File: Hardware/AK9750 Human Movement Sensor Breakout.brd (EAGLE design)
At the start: 25.4 x 25.4 mm, 27 parts, among them J2 SMD, J3 PTH, J4 SMD, U2 AK9750

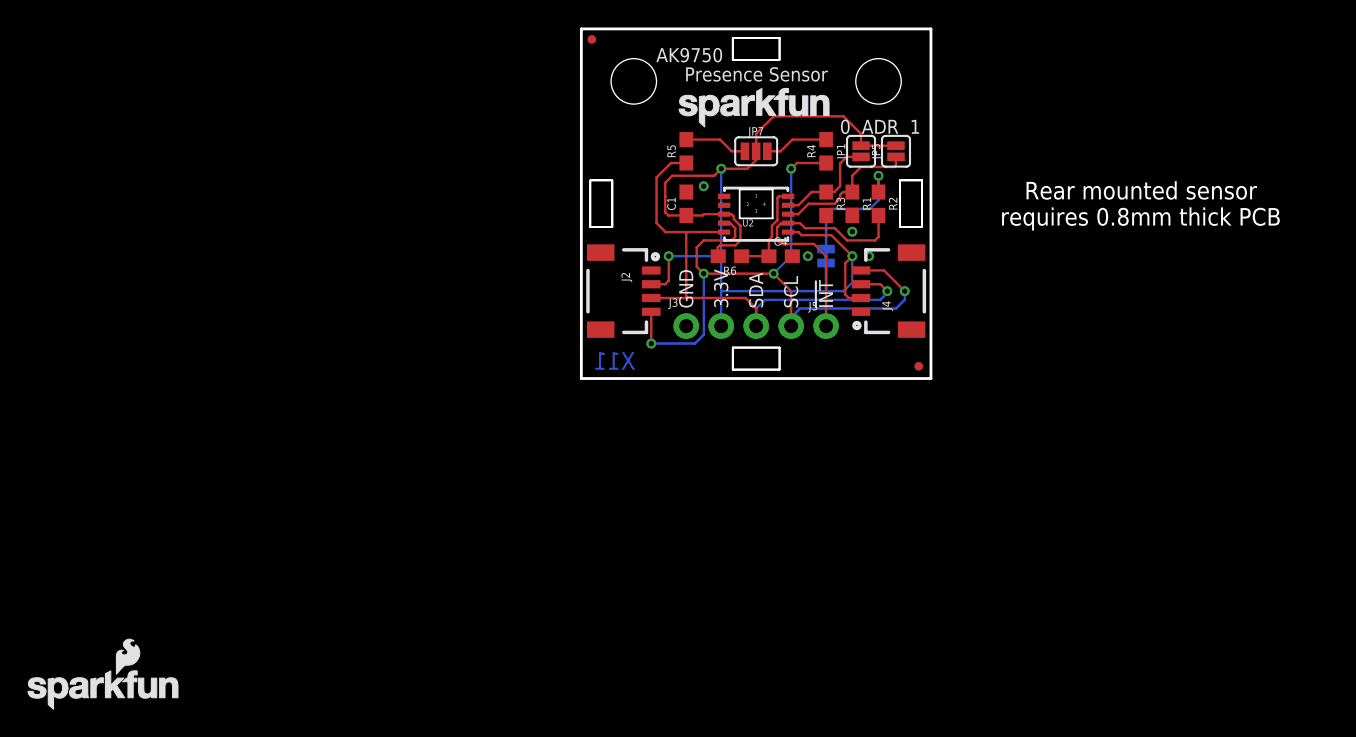
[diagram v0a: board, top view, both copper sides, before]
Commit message: Changed sensor to AK9753
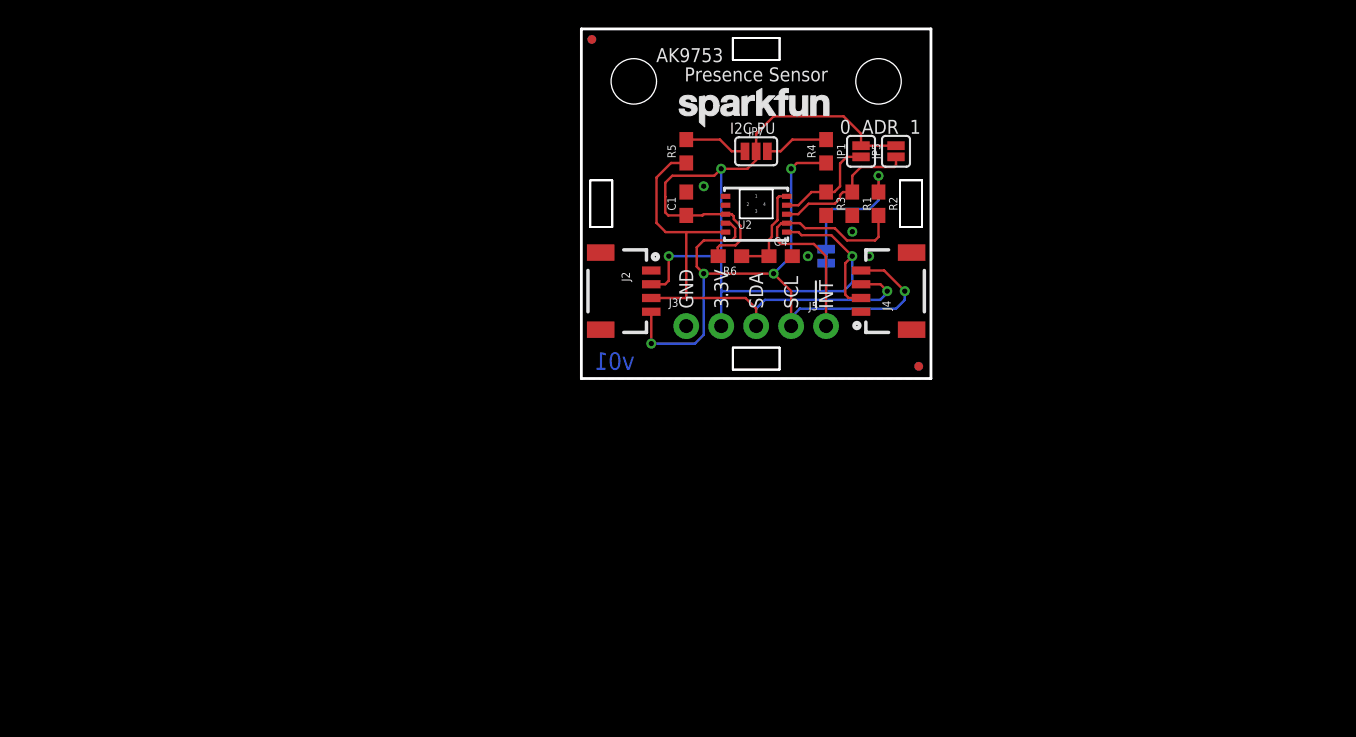
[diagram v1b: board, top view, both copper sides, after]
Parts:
- added JP10, JP9: FIDUCIALUFIDUCIAL, SparkFun:MICRO-FIDUCIAL
- added LOGO3: REVISION, SparkFun-Aesthetics:REVISION
- J2, J4: value SMD -> Qwiic Right Angle; device SparkX:1X04_1MM_RA -> SparkFun-Connectors:1X04_1MM_RA
- J3: device SparkX:1X04_NO_SILK -> SparkFun-Connectors:1X04_NO_SILK
- LOGO2: value SFE_LOGO_NAME_FLAME.1_INCH -> SFE_LOGO_NAME.1_INCH; device SparkFun-Aesthetics:SFE_LOGO_NAME_FLAME_.1 -> SparkFun-Aesthetics:SFE_LOGO_NAME_.1
- U$1: device SparkFun-Aesthetics:SFE_LOGO_NAME_.1 -> SparkFun-Aesthetics:ORDERING_INSTRUCTIONS
- U2: value AK9750 -> AK9753; device SparkX:SON10 -> SparkFun-Sensors:SON10
- moved LOGO2 63.2 mm to (6.60, 17.8)
- moved U$1 59.5 mm to (-36.8, -22.9)
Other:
- board text added: "A. England"
- board text added: "AK9753"
- board text added: "I2C PU"
- board text added: "JP8"
- board text added: "v01"
- board text removed: "AK9750"
- board text removed: "X11"

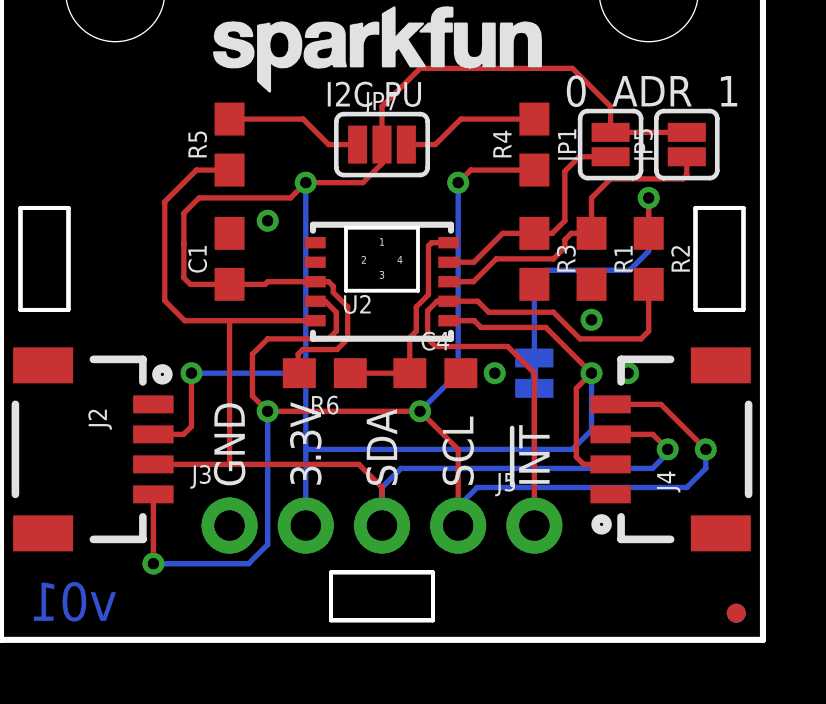
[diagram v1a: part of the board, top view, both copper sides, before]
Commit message: Moved pins to fit Arduino I2C layout, fixed JP8 silk
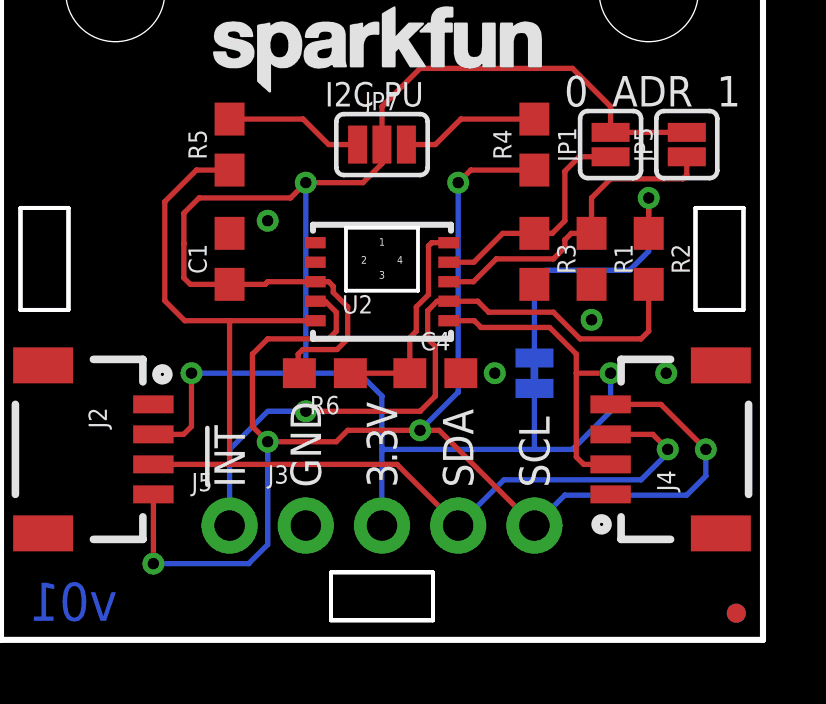
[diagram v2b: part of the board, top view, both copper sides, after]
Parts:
- moved J5 10.2 mm to (7.62, 3.81)
- moved J3 2.54 mm to (10.2, 3.81)
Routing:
- net !INT: track 19.7 -> 22.8 mm, vias 0 -> 1
- net SDA: track 38.7 -> 37.2 mm
- net SCL: track 51.7 -> 50.5 mm
- net 3.3V: track 75.9 -> 76.6 mm
